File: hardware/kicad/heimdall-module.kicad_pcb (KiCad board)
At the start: 2 copper layers, 56.4 x 40.9 mm, 36 parts, among them J2 Breakout, U1 MC33269DT-3.3G, U2 ESP32-C3-WROOM-02-N4, U3 TYPEC-214-ARP14H105, U4 USBLC6-2SC6, U5 74LVC1G34

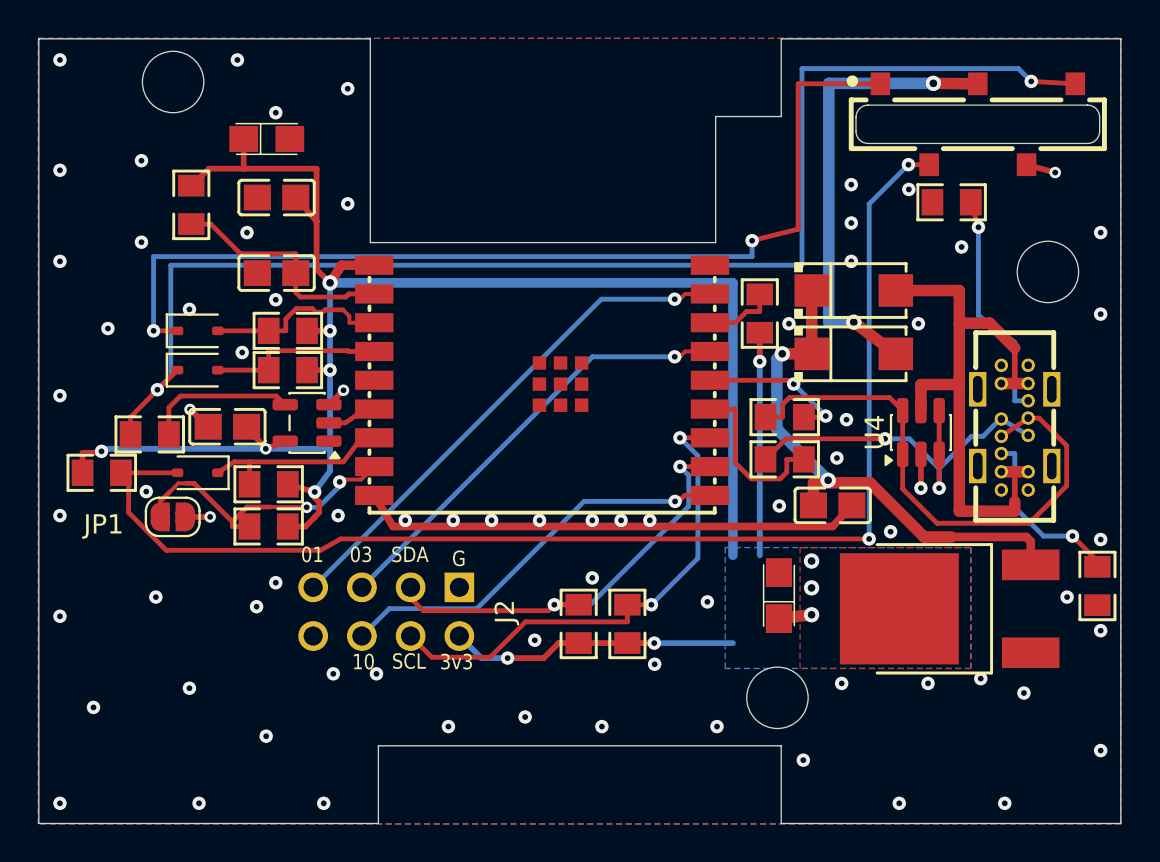
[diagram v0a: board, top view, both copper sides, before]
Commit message: Fit the case's lid bosses, M2 screws, spread parts for hand soldering
Case fit (measured on the printed case):
- Board corners chamfered 45 deg (2.8mm legs): the lid screw bosses
  (1.7mm holes, 3.5mm bosses in the cavity corners) stopped the board
  on its way down to the standoffs. ~0.47mm left to each boss.
- MH1-MH3 3.2mm (M3) -> 2.2mm for 2mm self-tapping screws into the
  standoffs' 1.8mm pilots; the lid uses the same screws. Copper keepout
  stays 3mm.

Layout (spread_place.py, then the route_pcb.py flow re-run in full):
- Left of the module: >= 1mm between courtyards, parts in module pin
  order; HB and BOOT parts moved below the module, left of J1.
- U1 at the bottom edge with its heatsink copper; C1/C2 beside it.
- R3/R4 off the module and turned 180, D1 up from D2, R9/R10 apart.
- Hand routes for VCC, HB, SIGNAL, DATA redrawn; 3V3 junction via by
  module pin 1 0.7/0.3 so EN runs straight; U5 GND via.

Silkscreen and numbering:
- All reference designators on top silk, 1.0mm (silk_refs.py).
- Renumbered without gaps: J2->J1, D6->D5, R8..R17->R5..R14
  (bay_pcb.py, rev_pcb.py, case_place.py keep the names of their time).

Export: jlc_export.py (from heimdall-switch) writes the Gerber/drill
package to hardware/kicad/gerber/ (ignored); board plot settings now
Protel extensions, mask subtracted from silk.

ERC 0. DRC 0 unconnected, 0 parity; 2 starved-thermal warnings on U3
A1/A12 as before.

Co-Authored-By: Claude Opus 5.5 <noreply@anthropic.com>
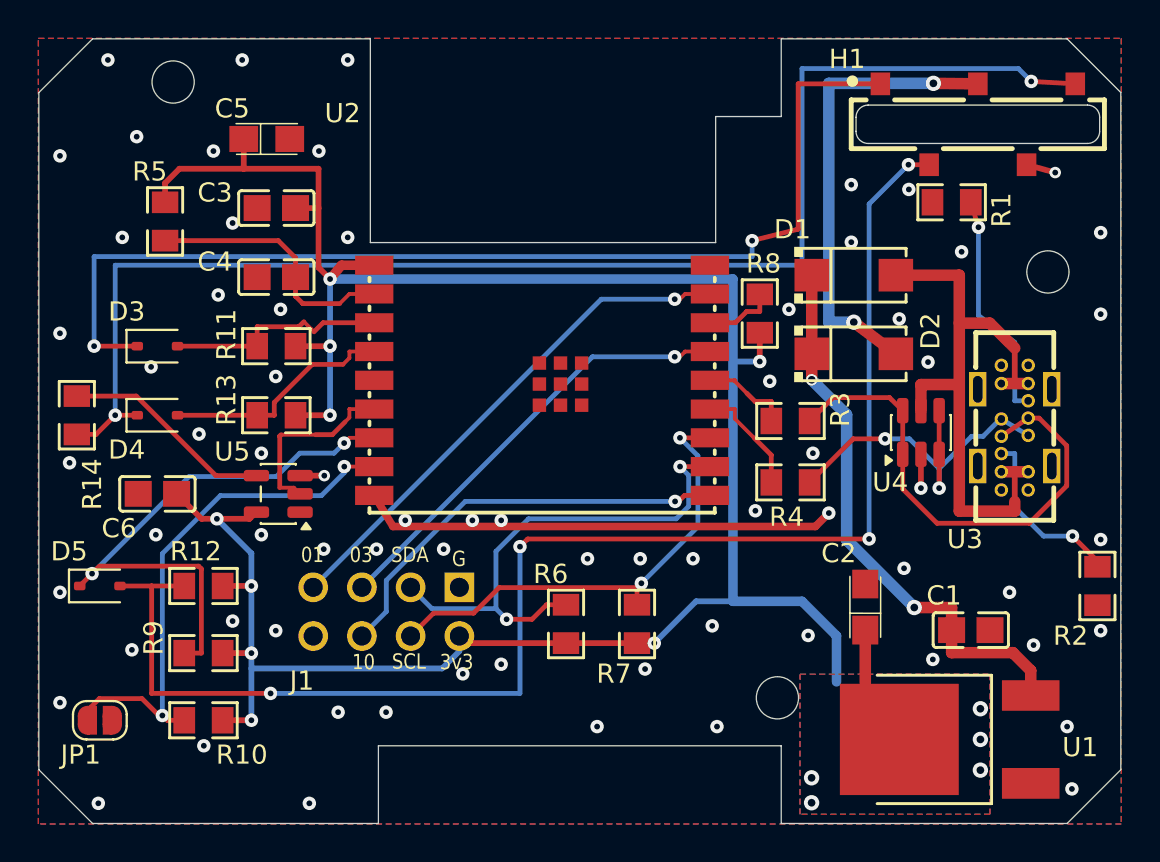
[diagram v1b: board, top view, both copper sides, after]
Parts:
- MH1, MH2, MH3: value M3 -> M2; footprint MountingHole:MountingHole_3.2mm_M3_ISO14580 -> MountingHole:MountingHole_2.2mm_M2_ISO14580
- moved JP1 11.3 mm to (122.6, 125.0)
- moved R10 10.7 mm to (128.0, 125.0)
- moved C1 9.70 mm to (168.0, 120.3)
- moved R9 9.43 mm to (128.0, 121.5)
- moved R12 7.93 mm to (128.0, 118.0), turned to 180 degrees
- moved D5 7.80 mm to (122.6, 118.0), turned to 0 degrees
- moved U1 6.81 mm to (167.7, 126.0)
- moved C6 5.06 mm to (125.6, 113.2)
- moved C2 4.54 mm to (162.5, 119.1)
- moved U5 3.99 mm to (131.9, 113.2)
- moved R14 3.93 mm to (121.4, 109.1), turned to 90 degrees
- moved D4 3.15 mm to (125.6, 109.1)
- moved R13 2.43 mm to (131.8, 109.1)
- moved D3 2.25 mm to (125.6, 105.5)
- moved R5 1.62 mm to (126.0, 99.0)
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- renumbered D6 to D5, J2 to J1, R13 to R10, R14 to R11, R15 to R12, R16 to R13, R17 to R14, R8 to R5, R9 to R6, R10 to R7, R11 to R8, R12 to R9
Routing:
- net /HB_OUT: track 10.0 -> 29.8 mm, vias 0 -> 2
- net /VCC: track 117.5 -> 131.4 mm, vias 12 -> 14
- net /IO9: track 15.7 -> 27.8 mm
- net /HB: track 66.0 -> 75.6 mm, vias 2 -> 4
- net /DATA_TX: track 2.56 -> 9.66 mm
- net /SIGNAL: track 51.5 -> 56.4 mm
- net /SDA: track 22.7 -> 26.9 mm
- net GND: track 33.3 -> 29.5 mm, vias 74 -> 70
- net Net-(U2-IO19): track 7.97 -> 4.70 mm, vias 2 -> 0
- net /DATA_DRV: track 7.89 -> 11.1 mm
- net /DATA: track 68.8 -> 72.0 mm
- net /DATA_RX: track 9.19 -> 12.2 mm
- net Net-(U2-IO18): track 8.86 -> 5.90 mm
- net /USB-D+: track 28.8 -> 26.2 mm
- net /PPM_IN: track 9.59 -> 11.8 mm
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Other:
- outline, holes or cut-outs redrawn
